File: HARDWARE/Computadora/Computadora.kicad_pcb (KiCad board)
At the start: 2 copper layers, 82 x 87 mm, 45 parts, among them IC1 ATMEGA328-P, J1 DB9, K1 AUX_PINS, P1 MOTORS PWM OUTPUT, P2 CONN_2, P3 CONN_SENSORES, Q1 BS170, Q2 BS170, SW1 RESET, U1 MAX232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

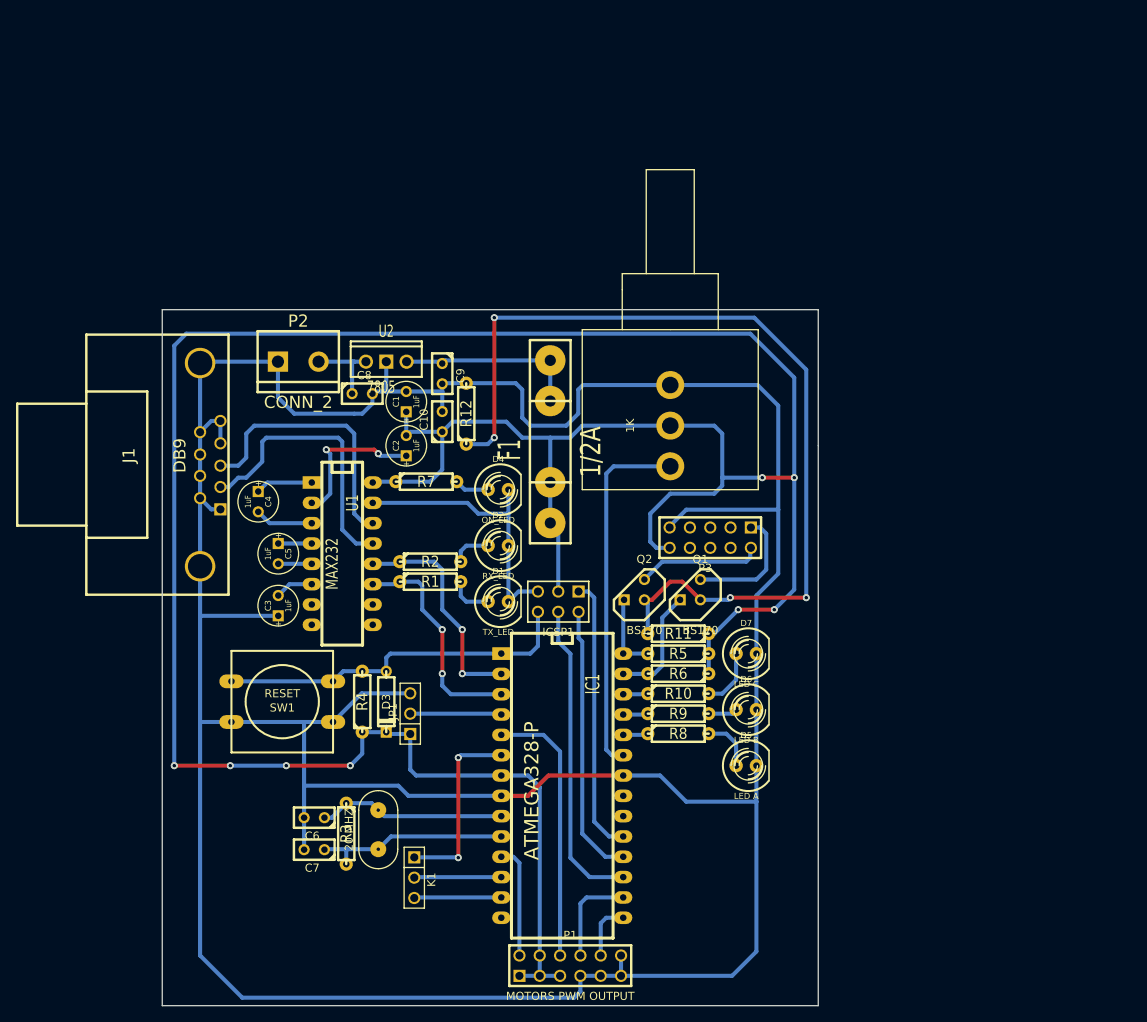
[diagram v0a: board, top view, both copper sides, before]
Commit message: Se hace una nueva placa y circuito esquemático separando los motores
Signed-off-by: Gonzalo Nahuel Vaca <vacagonzalo@gmail.com>
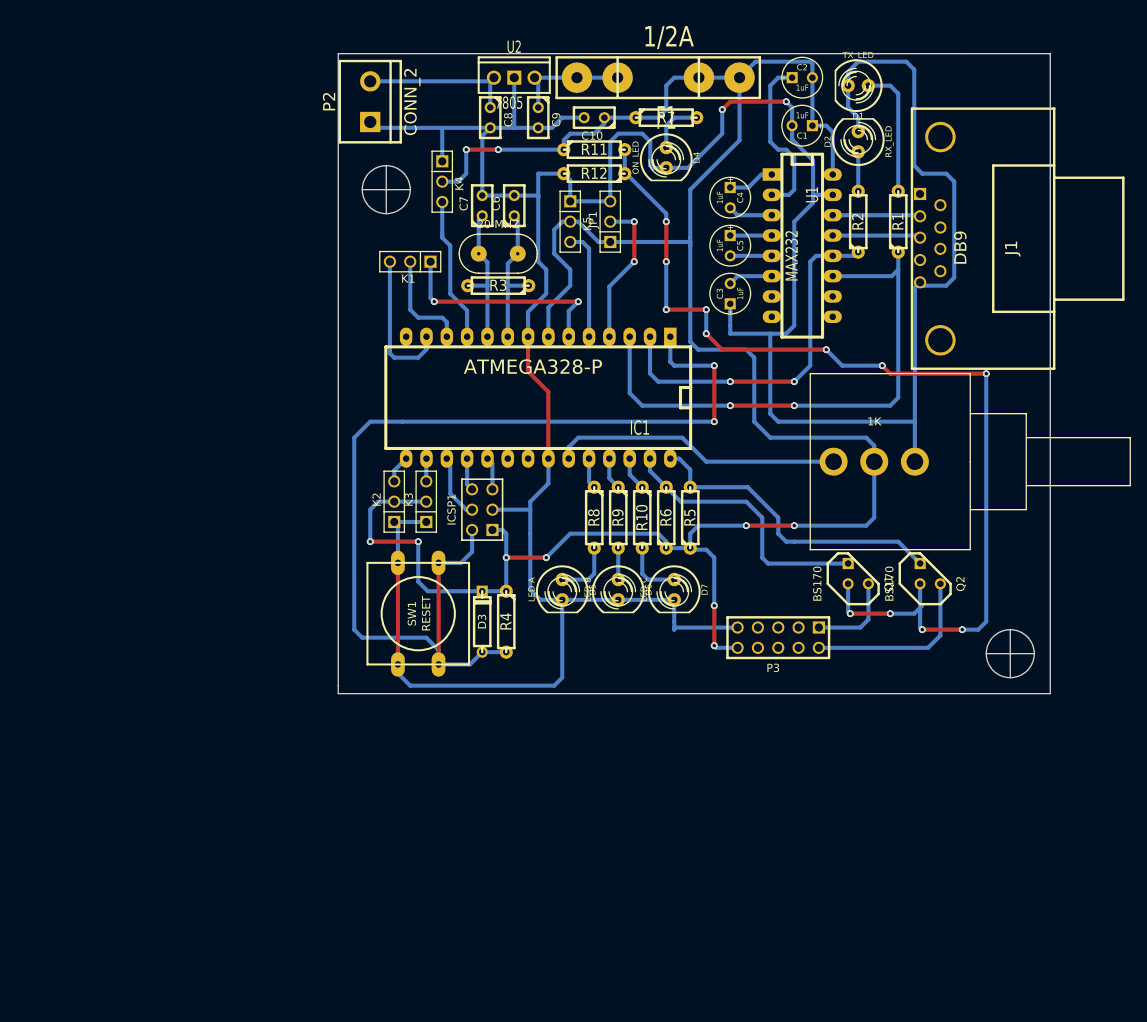
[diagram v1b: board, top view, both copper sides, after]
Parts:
- removed P1: MOTORS PWM OUTPUT, pin_array_6x2corregido
- added K2: CONN_3, PIN_ARRAY_3X1, F.Cu at (135.0, 83.0)
- added K3: CONN_3, PIN_ARRAY_3X1, F.Cu at (139.0, 83.0)
- added K4: CONN_3, PIN_ARRAY_3X1, F.Cu at (141.0, 43.0)
- added K5: CONN_3, PIN_ARRAY_3X1, F.Cu at (157.0, 48.0)
- J1: footprint DB9FCcorregido -> DB9FC
- moved J1 94.4 mm to (202.0, 50.0), turned to 270 degrees
- moved C7 83.2 mm to (146.0, 46.0), turned to 90 degrees
- moved C6 80.5 mm to (150.0, 46.0), turned to 90 degrees
- moved D1 78.6 mm to (193.0, 31.0), turned to 180 degrees
- moved K1 77.0 mm to (137.0, 53.0), turned to 180 degrees
- moved R1 73.8 mm to (198.0, 48.0), turned to 90 degrees
- moved X1 73.5 mm to (148.0, 52.0), turned to 0 degrees
- moved R3 71.1 mm to (148.0, 56.0), turned to 180 degrees
- moved C4 70.2 mm to (177.0, 45.0)
- moved U1 69.2 mm to (186.0, 51.0)
- moved C3 68.7 mm to (177.0, 57.0)
- moved C5 68.4 mm to (177.0, 51.0)
- moved R2 68.3 mm to (193.0, 48.0), turned to 90 degrees
- moved D2 67.6 mm to (193.0, 38.0), turned to 90 degrees
- moved C2 67.6 mm to (186.0, 30.0), turned to 0 degrees
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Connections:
- ICSP1 pad 1: /SCK -> +5V
- ICSP1 pad 2: /MISO -> /RESET
- ICSP1 pad 3: +5V -> GND
- ICSP1 pad 5: GND -> /SCK
- ICSP1 pad 6: /RESET -> /MISO
- J1 pad : GND -> (no net)
- J1 pad 1: GND -> (no net)
- J1 pad 3: N-0000046 -> N-0000044
- J1 pad 4: GND -> (no net)
- J1 pad 6: GND -> (no net)
- J1 pad 7: GND -> (no net)
- J1 pad 8: GND -> (no net)
- J1 pad 9: GND -> (no net)
- U1 pad 13: N-0000045 -> N-0000044
- U1 pad 14: N-0000046 -> N-0000045
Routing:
- net GND: track 489.5 -> 397.7 mm, vias 0 -> 2
- net /RESET: track 45.4 -> 128.3 mm, vias 0 -> 2
- net +5V: track 371.5 -> 296.7 mm, vias 8 -> 10
- net /TX: track 27.9 -> 68.4 mm
- net N-0000046: track 33.8 -> 0.00 mm
- net /MOSI: track 39.0 -> 8.12 mm
- net /SCK: track 34.7 -> 4.10 mm
- net /MISO: track 34.2 -> 4.10 mm
- net /SCL: track 9.84 -> 39.1 mm
- net N-0000045: track 35.0 -> 11.0 mm
- net /PWM4: track 33.7 -> 13.7 mm
- net /SDA: track 14.5 -> 34.0 mm
- net /RX: track 28.1 -> 45.4 mm
- net N-0000044: track 0.00 -> 11.0 mm
- net N-0000059: track 5.52 -> 16.3 mm
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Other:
- board size 82 x 87 mm -> 89 x 80 mm
- rule pad_to_mask_clearance: 0 -> 0.2
